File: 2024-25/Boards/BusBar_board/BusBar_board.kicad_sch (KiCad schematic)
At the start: 22 parts

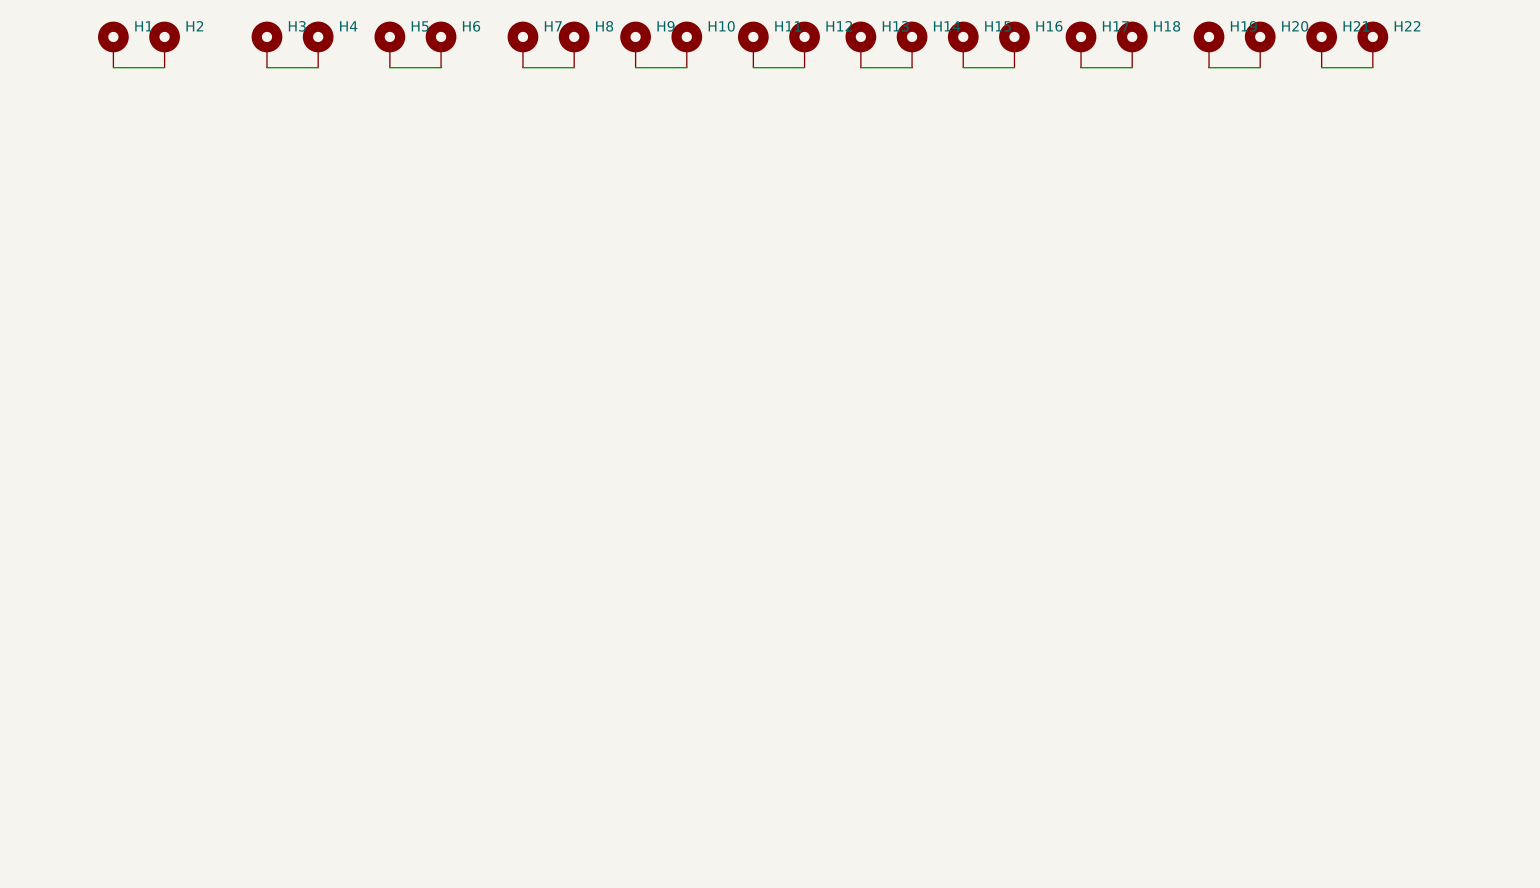
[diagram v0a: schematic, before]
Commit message: cell tape fuses added
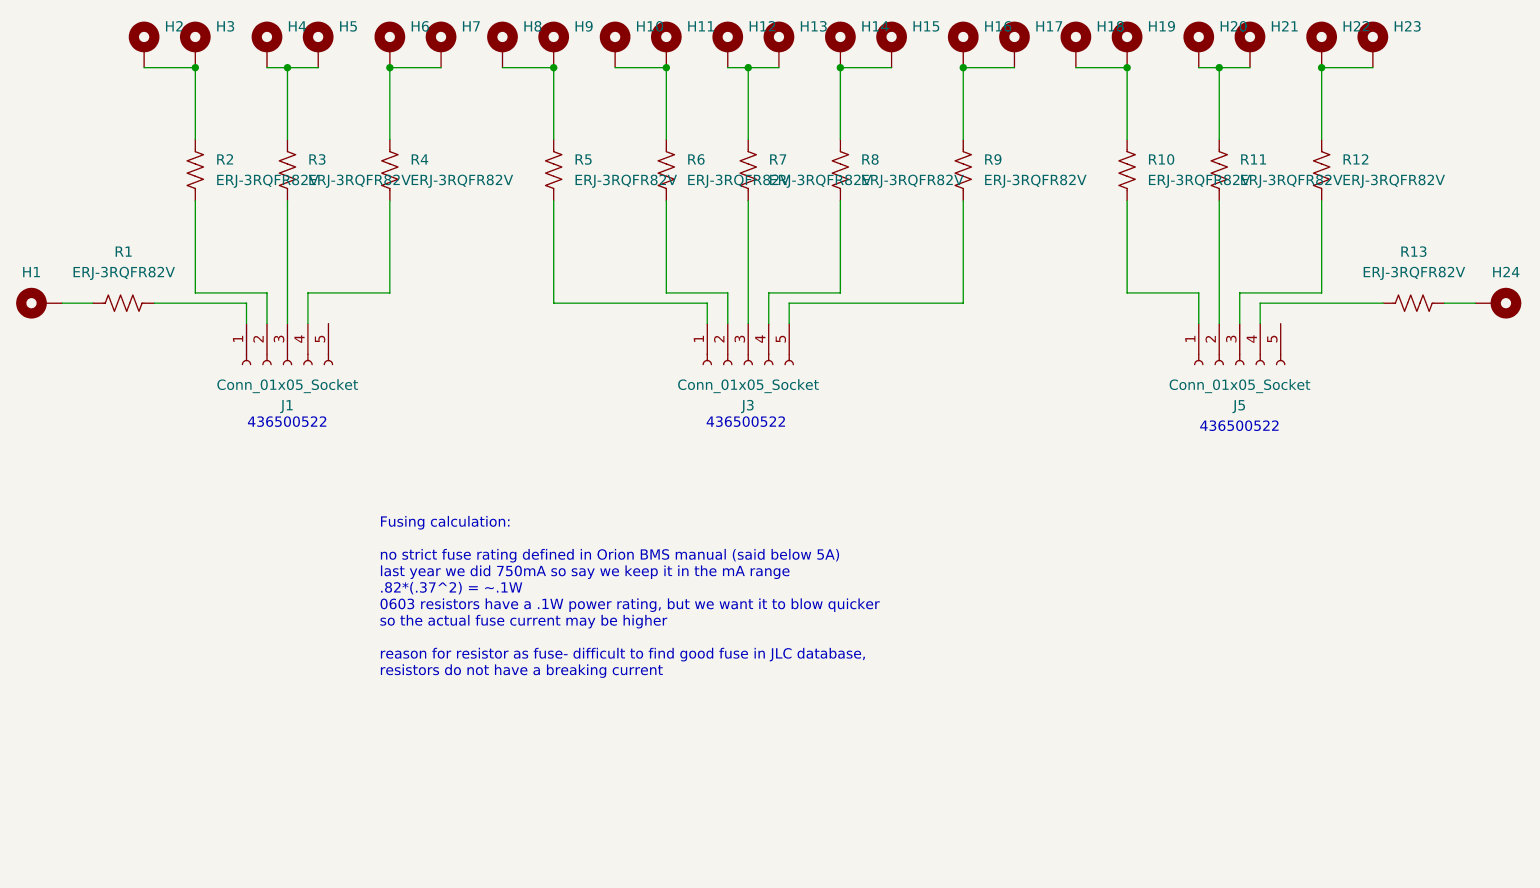
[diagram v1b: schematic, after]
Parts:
- added H1, H24: MountingHole_Pad, MountingHole:MountingHole_5.3mm_M5_Pad_Via, symbol Mechanical:MountingHole_Pad
- added J1, J3, J5: Conn_01x05_Socket, symbol Connector:Conn_01x05_Socket
- added R1, R10, R11, R12, R13, R2, R3, R4, R5, R6, R7, R8, R9: ERJ-3RQFR82V, Resistor_SMD:R_0603_1608Metric_Pad0.98x0.95mm_HandSolder, symbol Device:R_US
- renumbered H9 to H10, H10 to H11, H11 to H12, H12 to H13, H13 to H14, H14 to H15, H15 to H16, H16 to H17, H17 to H18, H18 to H19, H1 to H2, H19 to H20, H20 to H21, H21 to H22, H22 to H23, H2 to H3, H3 to H4, H4 to H5, H5 to H6, H6 to H7, H7 to H8, H8 to H9
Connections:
- net at H22.1, H23.1: now also R12.1
- net at H4.1, H5.1: now also R3.1
- net at H16.1, H17.1: now also R9.1
- net at H20.1, H21.1: now also R11.1
- net at H2.1, H3.1: now also R2.1
- net at H6.1, H7.1: now also R4.1
- net at H12.1, H13.1: now also R7.1
- net at H18.1, H19.1: now also R10.1
- net at H8.1, H9.1: now also R5.1
- net at H10.1, H11.1: now also R6.1
- net at H14.1, H15.1: now also R8.1
- new net: J5.1 (Pin_1), R10.2
- new net: J5.2 (Pin_2), R11.2
- new net: J5.3 (Pin_3), R12.2
- new net: J5.4 (Pin_4), R13.1
- new net: J1.2 (Pin_2), R2.2
- new net: H24.1, R13.2
- new net: J3.1 (Pin_1), R5.2
- new net: J3.2 (Pin_2), R6.2
- new net: J3.3 (Pin_3), R7.2
- new net: J3.4 (Pin_4), R8.2
- new net: J3.5 (Pin_5), R9.2
- new net: J1.3 (Pin_3), R3.2
- new net: H1.1, R1.1
- new net: J1.4 (Pin_4), R4.2
- new net: J1.1 (Pin_1), R1.2
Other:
- note added: "436500522"
- note added: "Fusing calculation: no strict fuse rating defined in Orion BMS manual (said below 5A) last year we did 750mA so say we keep it in the mA range .82*(.37^2) = ~.1W 0603 resistors have a .1W power rating, but we want it to blow quicker so the actual fuse current may be higher reason for resistor as fuse- difficult to find good fuse in JLC database, resistors do not have a breaking current"
- moved on the sheet: H10, H11, H12, H13, H14, H15, H18, H19, H2, H20, H21, H3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

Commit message: Cell tap routing + thicker bars
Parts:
- J1, J3, J5: footprint (none) -> Connector_Wago:Wago_734-135_1x05_P3.50mm_Vertical
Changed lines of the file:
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@@
 			)
 		)
-		(property "Footprint" ""
+		(property "Footprint" "Connector_Wago:Wago_734-135_1x05_P3.50mm_Vertical"
 			(at 209.55 113.03 0)
 			(effects
@@
 			)
 		)
-		(property "Footprint" ""
+		(property "Footprint" "Connector_Wago:Wago_734-135_1x05_P3.50mm_Vertical"
 			(at 148.59 113.03 0)
 			(effects
@@
 			)
 		)
-		(property "Footprint" ""
+		(property "Footprint" "Connector_Wago:Wago_734-135_1x05_P3.50mm_Vertical"
 			(at 91.44 113.03 0)
 			(effects

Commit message: checkbox schm
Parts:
- removed J3: Conn_01x05_Socket, Connector_Wago:Wago_734-135_1x05_P3.50mm_Vertical, symbol Connector:Conn_01x05_Socket
- added J2: Conn_01x05_Socket, Connector_Molex:Molex_PicoBlade_53398-0571_1x05-1MP_P1.25mm_Vertical, symbol Connector:Conn_01x05_Socket
- J1, J5: footprint Connector_Wago:Wago_734-135_1x05_P3.50mm_Vertical -> Connector_Molex:Molex_PicoBlade_53398-0571_1x05-1MP_P1.25mm_Vertical
- R1, R10, R11, R12, R13, R2, R3, R4, R5, R6, R7, R8, R9: value ERJ-3RQFR82V -> RL0805FR-070R25L; footprint Resistor_SMD:R_0603_1608Metric_Pad0.98x0.95mm_HandSolder -> Resistor_SMD:R_0805_2012Metric_Pad1.20x1.40mm_HandSolder
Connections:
- net at R5.2: now also J2.1 (Pin_1)
- net at R6.2: now also J2.2 (Pin_2)
- net at R7.2: now also J2.3 (Pin_3)
- net at R8.2: now also J2.4 (Pin_4)
- net at R9.2: now also J2.5 (Pin_5)
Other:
- note added: "Fusing calculation: no strict fuse rating defined in Orion BMS manual (said below 5A) last year we did 750mA so say we keep it in the mA range .250*(.707^2) = ~.125W 0805 resistors have a .125W power rating (have higher voltage ratings than smaller packages) we want it to blow quick so the actual fuse current may be higher than calculated reason for resistor as fuse- difficult to find good fuse i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"
- note removed: "436500522"
- note removed: "Fusing calculation: no strict fuse rating defined in Orion BMS manual (said below 5A) last year we did 750mA so say we keep it in the mA range .82*(.37^2) = ~.1W 0603 resistors have a .1W power rating, but we want it to blow quicker so the actual fuse current may be higher reason for resistor as fuse- difficult to find good fuse in JLC database, resistors do not have a breaking current"
